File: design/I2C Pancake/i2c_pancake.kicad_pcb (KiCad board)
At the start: 4 copper layers, 74.9 x 45 mm, 44 parts, among them J1 Conn_01x03, J2 Conn_01x03, J3 Conn_01x05_Male, J4 Conn_01x04, J5 Conn_01x04, J6 Conn_01x04, J7 Conn_01x05_Male, J8 Conn_01x05_Female, SW1 SW_DIP_x04, U1 INA826, U2 TL750M10CKVU, U3 INA826, U4 INA826, U6 PIC16F1826-ISO

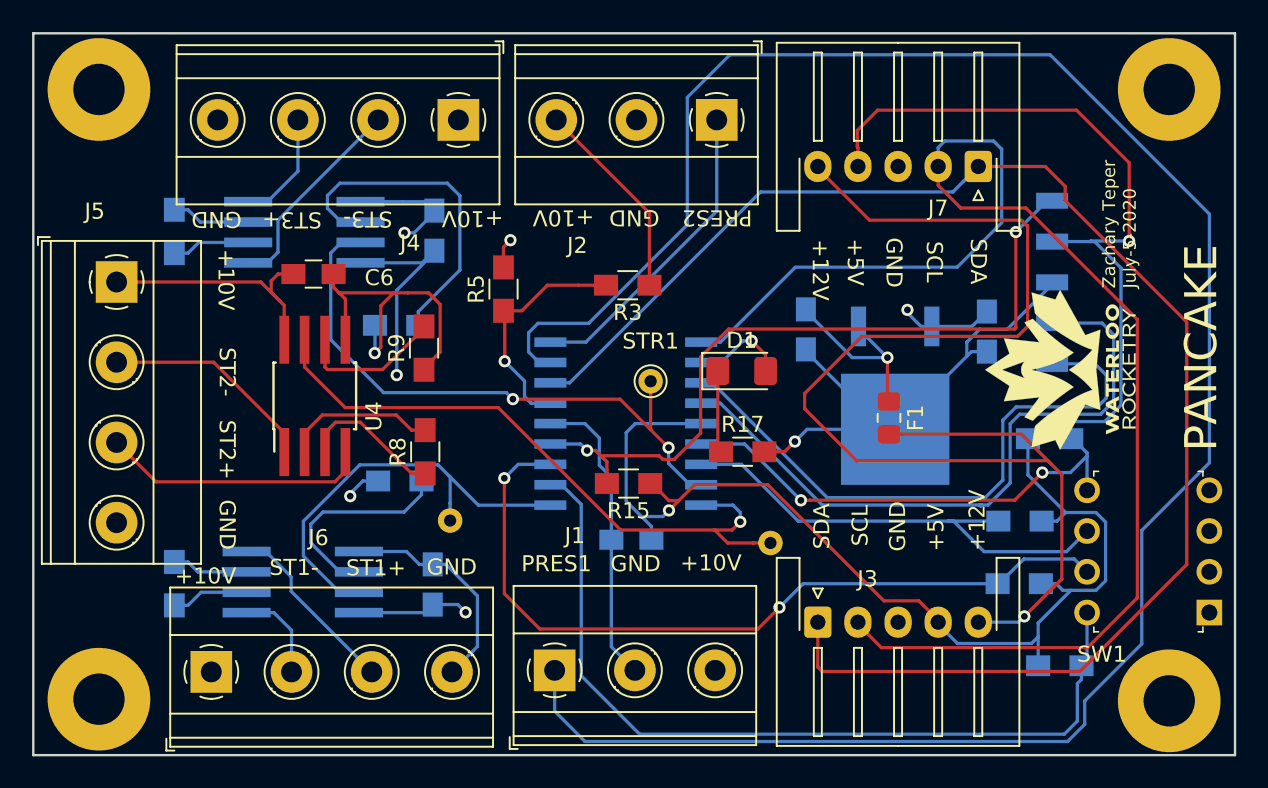
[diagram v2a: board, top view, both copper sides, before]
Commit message: Implement improvements suggested by Jared
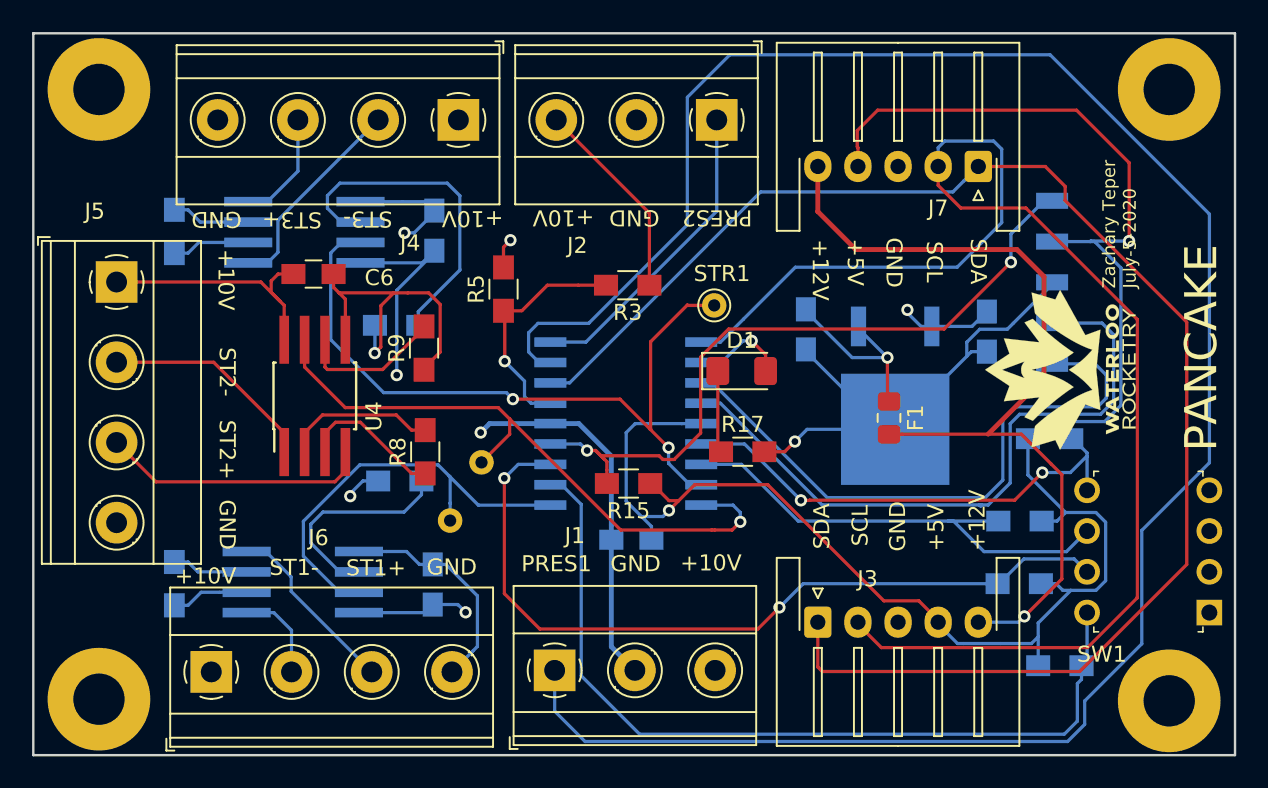
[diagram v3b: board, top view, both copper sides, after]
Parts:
- moved STR2 21.1 mm to (117.6, 113.0), turned to 180 degrees
- moved STR1 6.17 mm to (132.1, 103.2)
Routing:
- net +12V: track 79.0 -> 55.1 mm
- net /STRAIN_OUT_1: track 37.9 -> 45.3 mm
- net GND: track 99.5 -> 103.9 mm, vias 5 -> 6
- net /~MCLR: track 47.9 -> 45.8 mm
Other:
- net class Power added: clearance 0.254, trace_width 0.3048, via_dia 0.762, via_drill 0.4191

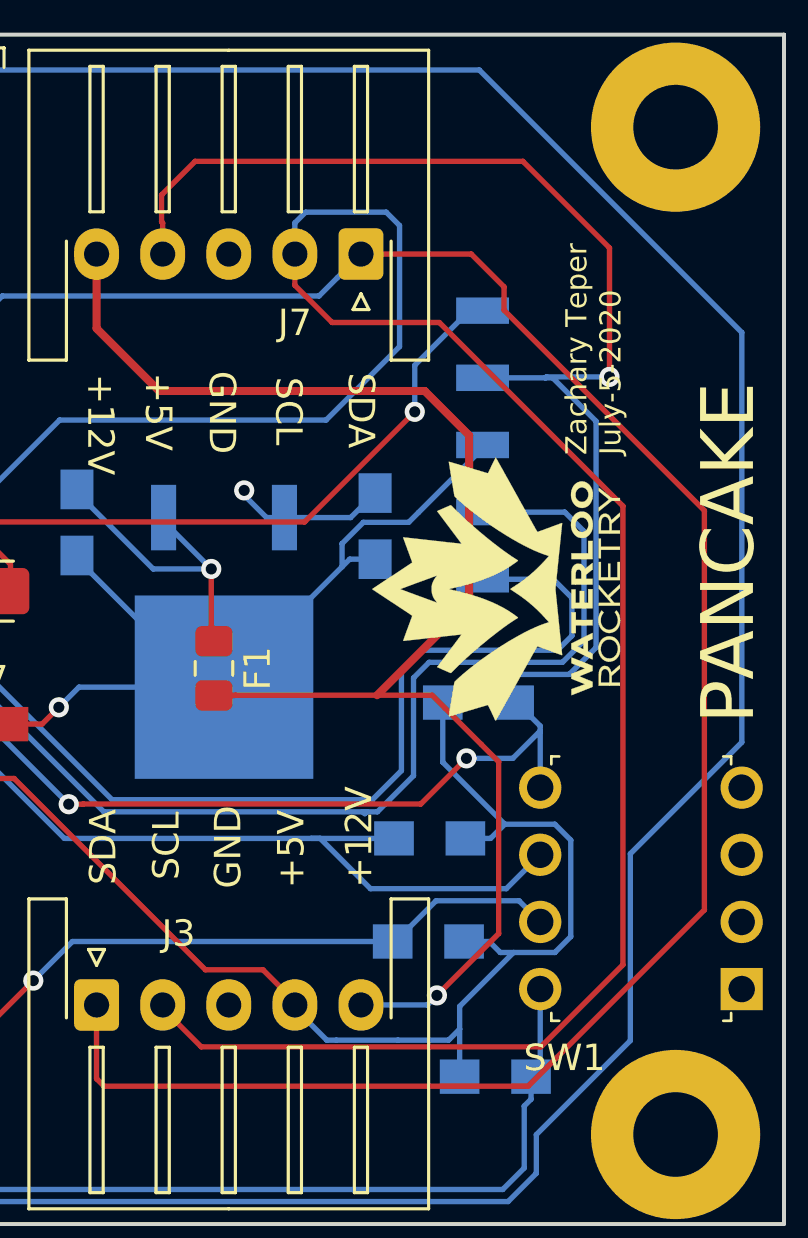
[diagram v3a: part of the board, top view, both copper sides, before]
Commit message: Replace +5V and +12V routing with 12 traces
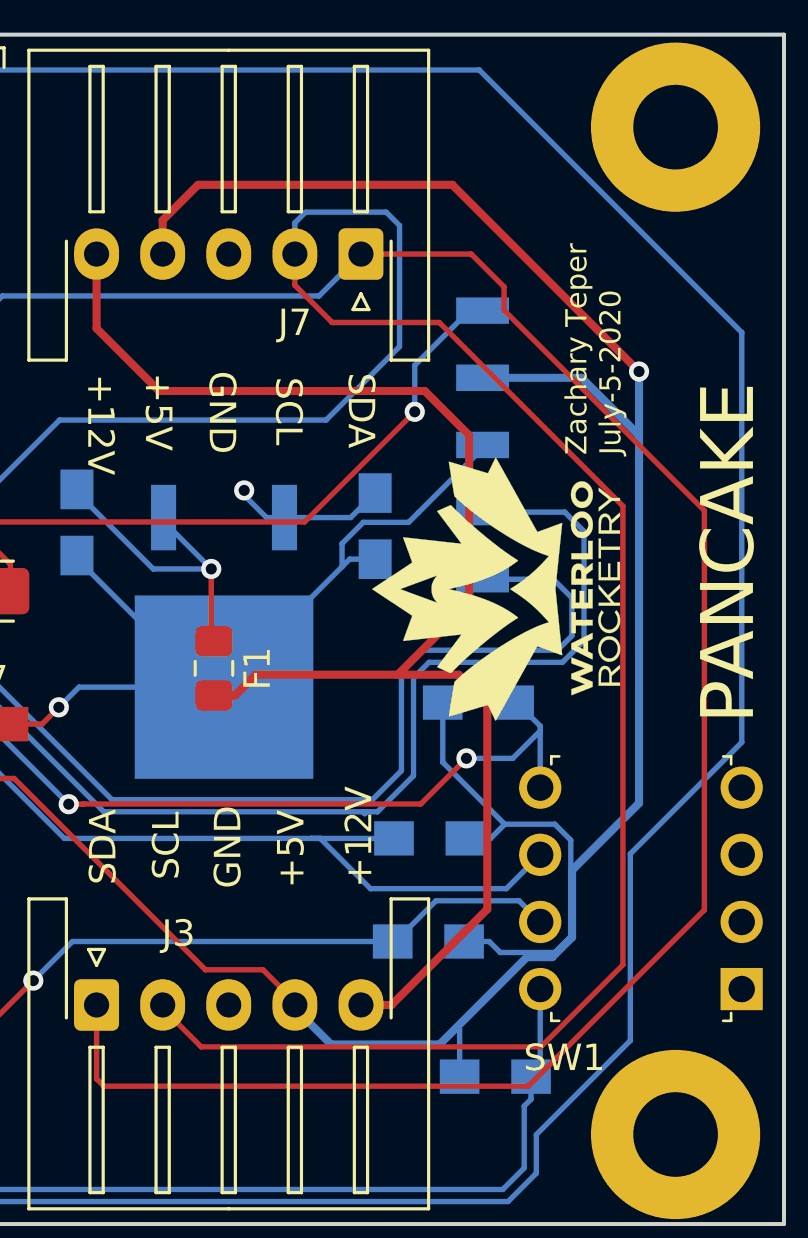
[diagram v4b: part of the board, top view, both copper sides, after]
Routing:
- net +5V: track 116.9 -> 123.9 mm
- net +12V: track 55.1 -> 54.5 mm, vias 1 -> 0
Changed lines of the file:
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@@
     (thickness 1.6)
     (drawings 40)
-    (tracks 477)
+    (tracks 464)
     (zones 0)
     (modules 44)
@@
   (segment (start 142.8924 111.6327) (end 142.994 111.7343) (width 0.2032) (layer F.Cu) (net 20))
   (segment (start 142.8924 109.4626) (end 142.8924 111.6327) (width 0.2032) (layer F.Cu) (net 20))
-  (segment (start 152.454 128.4976) (end 152.2866 128.665) (width 0.2032) (layer B.Cu) (net 21))
   (segment (start 153.4572 119.653) (end 152.504 119.653) (width 0.2032) (layer B.Cu) (net 21))
   (segment (start 153.992801 119.117399) (end 153.4572 119.653) (width 0.2032) (layer B.Cu) (net 21))
@@
   (segment (start 153.4072 123.553) (end 153.822801 123.968601) (width 0.2032) (layer B.Cu) (net 21))
   (segment (start 152.454 123.553) (end 153.4072 123.553) (width 0.2032) (layer B.Cu) (net 21))
-  (segment (start 146.054 126.078) (end 146.054 125.953) (width 0.2032) (layer B.Cu) (net 21))
   (segment (start 147.25961 127.28361) (end 146.054 126.078) (width 0.2032) (layer B.Cu) (net 21))
   (segment (start 154.325001 123.968601) (end 155.888689 123.968601) (width 0.2032) (layer B.Cu) (net 21))
   (segment (start 153.822801 123.968601) (end 154.325001 123.968601) (width 0.2032) (layer B.Cu) (net 21))
-  (segment (start 154.325001 123.968601) (end 152.2866 126.007002) (width 0.2032) (layer B.Cu) (net 21))
   (segment (start 151.6478 116.772398) (end 151.6478 114.5172) (width 0.2032) (layer B.Cu) (net 21))
   (segment (start 153.992801 119.117399) (end 151.6478 116.772398) (width 0.2032) (layer B.Cu) (net 21))
-  (segment (start 151.7478 114.5172) (end 152.8146 113.4504) (width 0.2032) (layer B.Cu) (net 21))
-  (segment (start 151.6478 114.5172) (end 151.7478 114.5172) (width 0.2032) (layer B.Cu) (net 21))
-  (segment (start 152.8146 113.4504) (end 156.4306 113.4504) (width 0.2032) (layer B.Cu) (net 21))
-  (segment (start 156.4306 113.4504) (end 157.4466 112.4344) (width 0.2032) (layer B.Cu) (net 21))
-  (segment (start 157.4466 112.4344) (end 157.4466 103.8746) (width 0.2032) (layer B.Cu) (net 21))
-  (segment (start 157.4466 103.8746) (end 155.805 102.233) (width 0.2032) (layer B.Cu) (net 21))
-  (segment (start 141.054 96.3748) (end 141.0128 96.3336) (width 0.2032) (layer F.Cu) (net 21))
-  (segment (start 141.054 97.553) (end 141.054 96.3748) (width 0.2032) (layer F.Cu) (net 21))
-  (segment (start 141.0128 96.3336) (end 141.0128 95.3148) (width 0.2032) (layer F.Cu) (net 21))
-  (segment (start 141.0128 95.3148) (end 142.2828 94.0448) (width 0.2032) (layer F.Cu) (net 21))
-  (segment (start 142.2828 94.0448) (end 154.678 94.0448) (width 0.2032) (layer F.Cu) (net 21))
-  (via (at 157.9546 102.1982) (size 0.762) (drill 0.4191) (layers F.Cu B.Cu) (net 21))
-  (segment (start 154.678 94.0448) (end 157.9546 97.3214) (width 0.2032) (layer F.Cu) (net 21))
-  (segment (start 157.9546 97.3214) (end 157.9546 102.1982) (width 0.2032) (layer F.Cu) (net 21))
-  (segment (start 155.567 102.1982) (end 155.5322 102.233) (width 0.2032) (layer B.Cu) (net 21))
-  (segment (start 157.9546 102.1982) (end 155.567 102.1982) (width 0.2032) (layer B.Cu) (net 21))
-  (segment (start 155.805 102.233) (end 155.5322 102.233) (width 0.2032) (layer B.Cu) (net 21))
-  (segment (start 155.5322 102.233) (end 153.154 102.233) (width 0.2032) (layer B.Cu) (net 21))
   (segment (start 130.0824 113.5774) (end 131.2856 113.5774) (width 0.2032) (layer B.Cu) (net 21))
   (segment (start 127.17183 113.5774) (end 130.0824 113.5774) (width 0.2032) (layer B.Cu) (net 21))
@@
   (segment (start 128.1858 119.9882) (end 127.622 119.4244) (width 0.2032) (layer B.Cu) (net 21))
   (segment (start 127.622 119.4244) (end 126.610999 118.413399) (width 0.2032) (layer B.Cu) (net 21))
-  (segment (start 149.95201 127.28361) (end 147.62659 127.28361) (width 0.2032) (layer B.Cu) (net 21))
-  (segment (start 147.62659 127.28361) (end 147.25961 127.28361) (width 0.2032) (layer B.Cu) (net 21))
   (segment (start 146.054 125.828) (end 146.054 125.953) (width 0.2032) (layer F.Cu) (net 21))
   (segment (start 144.84839 124.62239) (end 146.054 125.828) (width 0.2032) (layer F.Cu) (net 21))
@@
   (segment (start 129.278 118.9876) (end 129.8749 118.3907) (width 0.2032) (layer F.Cu) (net 21))
   (segment (start 129.8749 118.3907) (end 130.8782 117.3874) (width 0.2032) (layer F.Cu) (net 21))
-  (segment (start 151.86839 127.28361) (end 152.2866 126.8654) (width 0.2032) (layer B.Cu) (net 21))
-  (segment (start 149.95201 127.28361) (end 151.86839 127.28361) (width 0.2032) (layer B.Cu) (net 21))
-  (segment (start 152.2866 126.007002) (end 152.2866 126.8654) (width 0.2032) (layer B.Cu) (net 21))
   (segment (start 152.2866 126.8654) (end 152.2866 128.665) (width 0.2032) (layer B.Cu) (net 21))
+  (segment (start 141.054 96.2732) (end 142.3934 94.9338) (width 0.3048) (layer F.Cu) (net 21))
+  (segment (start 141.054 97.553) (end 141.054 96.2732) (width 0.3048) (layer F.Cu) (net 21))
+  (via (at 159.0722 101.995) (size 0.762) (drill 0.4191) (layers F.Cu B.Cu) (net 21))
+  (segment (start 142.3934 94.9338) (end 152.011 94.9338) (width 0.3048) (layer F.Cu) (net 21))
+  (segment (start 152.011 94.9338) (end 159.0722 101.995) (width 0.3048) (layer F.Cu) (net 21))
+  (segment (start 155.785875 124.146599) (end 154.827601 124.146599) (width 0.3048) (layer B.Cu) (net 21))
+  (segment (start 156.540401 123.392073) (end 155.785875 124.146599) (width 0.3048) (layer B.Cu) (net 21))
+  (segment (start 156.540401 120.852073) (end 156.540401 123.392073) (width 0.3048) (layer B.Cu) (net 21))
+  (segment (start 159.0722 118.320274) (end 156.540401 120.852073) (width 0.3048) (layer B.Cu) (net 21))
+  (segment (start 154.827601 124.146599) (end 151.5284 127.4458) (width 0.3048) (layer B.Cu) (net 21))
+  (segment (start 146.054 126.078) (end 146.054 125.953) (width 0.3048) (layer B.Cu) (net 21))
+  (segment (start 147.4218 127.4458) (end 146.054 126.078) (width 0.3048) (layer B.Cu) (net 21))
+  (segment (start 151.5284 127.4458) (end 147.4218 127.4458) (width 0.3048) (layer B.Cu) (net 21))
+  (segment (start 156.8972 102.233) (end 159.0722 104.408) (width 0.3048) (layer B.Cu) (net 21))
+  (segment (start 153.154 102.233) (end 156.8972 102.233) (width 0.3048) (layer B.Cu) (net 21))
+  (segment (start 159.0722 101.995) (end 159.0722 104.408) (width 0.3048) (layer B.Cu) (net 21))
+  (segment (start 159.0722 104.408) (end 159.0722 118.320274) (width 0.3048) (layer B.Cu) (net 21))
   (via (at 134.4342 108.4212) (size 0.762) (drill 0.4191) (layers F.Cu B.Cu) (net 22))
   (segment (start 135.2978 110.3008) (end 135.2978 109.2848) (width 0.2032) (layer F.Cu) (net 22))
@@
   (segment (start 132.3228 115.1312) (end 132.5216 115.33) (width 0.2032) (layer F.Cu) (net 23))
   (segment (start 132.3228 110.3008) (end 132.3228 115.1312) (width 0.2032) (layer F.Cu) (net 23))
-  (via (at 151.4268 125.5916) (size 0.762) (drill 0.4191) (layers F.Cu B.Cu) (net 24))
-  (segment (start 148.554 125.953) (end 151.0654 125.953) (width 0.2032) (layer B.Cu) (net 24))
-  (segment (start 151.0654 125.953) (end 151.4268 125.5916) (width 0.2032) (layer B.Cu) (net 24))
-  (segment (start 153.7636 123.2548) (end 151.4268 125.5916) (width 0.2032) (layer F.Cu) (net 24))
-  (segment (start 153.7636 116.756318) (end 153.7636 123.2548) (width 0.2032) (layer F.Cu) (net 24))
-  (segment (start 151.716582 114.7093) (end 153.101241 116.093959) (width 0.2032) (layer F.Cu) (net 24))
-  (segment (start 153.101241 116.093959) (end 153.7636 116.756318) (width 0.2032) (layer F.Cu) (net 24))
-  (segment (start 143.794 114.2468) (end 143.803 114.2378) (width 0.2032) (layer F.Cu) (net 24))
-  (segment (start 142.994 114.2468) (end 143.794 114.2468) (width 0.2032) (layer F.Cu) (net 24))
-  (segment (start 151.245082 114.2378) (end 151.716582 114.7093) (width 0.2032) (layer F.Cu) (net 24))
-  (segment (start 149.1662 114.2378) (end 151.245082 114.2378) (width 0.2032) (layer F.Cu) (net 24))
-  (segment (start 143.803 114.2378) (end 149.1662 114.2378) (width 0.2032) (layer F.Cu) (net 24))
   (segment (start 138.554 97.553) (end 139.152168 97.553) (width 0.3048) (layer F.Cu) (net 24))
-  (segment (start 152.646 110.758) (end 149.1662 114.2378) (width 0.3048) (layer F.Cu) (net 24))
   (segment (start 152.646 104.411046) (end 152.646 110.758) (width 0.3048) (layer F.Cu) (net 24))
   (segment (start 150.966553 102.731599) (end 152.646 104.411046) (width 0.3048) (layer F.Cu) (net 24))
@@
   (segment (start 138.554 97.553) (end 138.554 100.3644) (width 0.3048) (layer F.Cu) (net 24))
   (segment (start 138.554 100.3644) (end 140.921199 102.731599) (width 0.3048) (layer F.Cu) (net 24))
+  (segment (start 153.330857 122.330943) (end 153.330857 114.541657) (width 0.3048) (layer F.Cu) (net 24))
+  (segment (start 148.554 125.953) (end 149.7088 125.953) (width 0.3048) (layer F.Cu) (net 24))
+  (segment (start 149.7088 125.953) (end 153.330857 122.330943) (width 0.3048) (layer F.Cu) (net 24))
+  (segment (start 152.2523 113.4631) (end 149.9409 113.4631) (width 0.3048) (layer F.Cu) (net 24))
+  (segment (start 153.330857 114.541657) (end 152.2523 113.4631) (width 0.3048) (layer F.Cu) (net 24))
+  (segment (start 152.646 110.758) (end 149.9409 113.4631) (width 0.3048) (layer F.Cu) (net 24))
+  (segment (start 144.5777 113.4631) (end 149.9409 113.4631) (width 0.3048) (layer F.Cu) (net 24))
+  (segment (start 143.794 114.2468) (end 144.5777 113.4631) (width 0.3048) (layer F.Cu) (net 24))
+  (segment (start 142.994 114.2468) (end 143.794 114.2468) (width 0.3048) (layer F.Cu) (net 24))
   (segment (start 149.510064 95.96839) (end 150.01361 96.471936) (width 0.2032) (layer B.Cu) (net 25))
   (segment (start 150.01361 96.471936) (end 150.01361 101.0531) (width 0.2032) (layer B.Cu) (net 25))

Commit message: Finish I2C Pancake board design and add gerbers!
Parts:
- STR2, STR3: moved to F.Cu
- turned STR2 to 0 degrees
- turned STR3 to 180 degrees
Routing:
- net /SDA: track 93.5 -> 101.0 mm, vias 0 -> 1
- net /SCL: track 85.7 -> 89.5 mm, vias 0 -> 3
- net +12V: track 54.5 -> 55.6 mm
- net +5V: track 123.9 -> 123.6 mm, vias 2 -> 1
